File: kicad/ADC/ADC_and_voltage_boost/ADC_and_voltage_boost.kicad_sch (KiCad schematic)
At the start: 11 parts, among them J1 Screw_Terminal_01x04, J2 Screw_Terminal_01x04, J3 Screw_Terminal_01x02, U4 MAX1032BEUG_

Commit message: v3 for ADC up
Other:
- moved on the sheet: A1, C1, C11, C2, C3, C8, C9, J2, U4

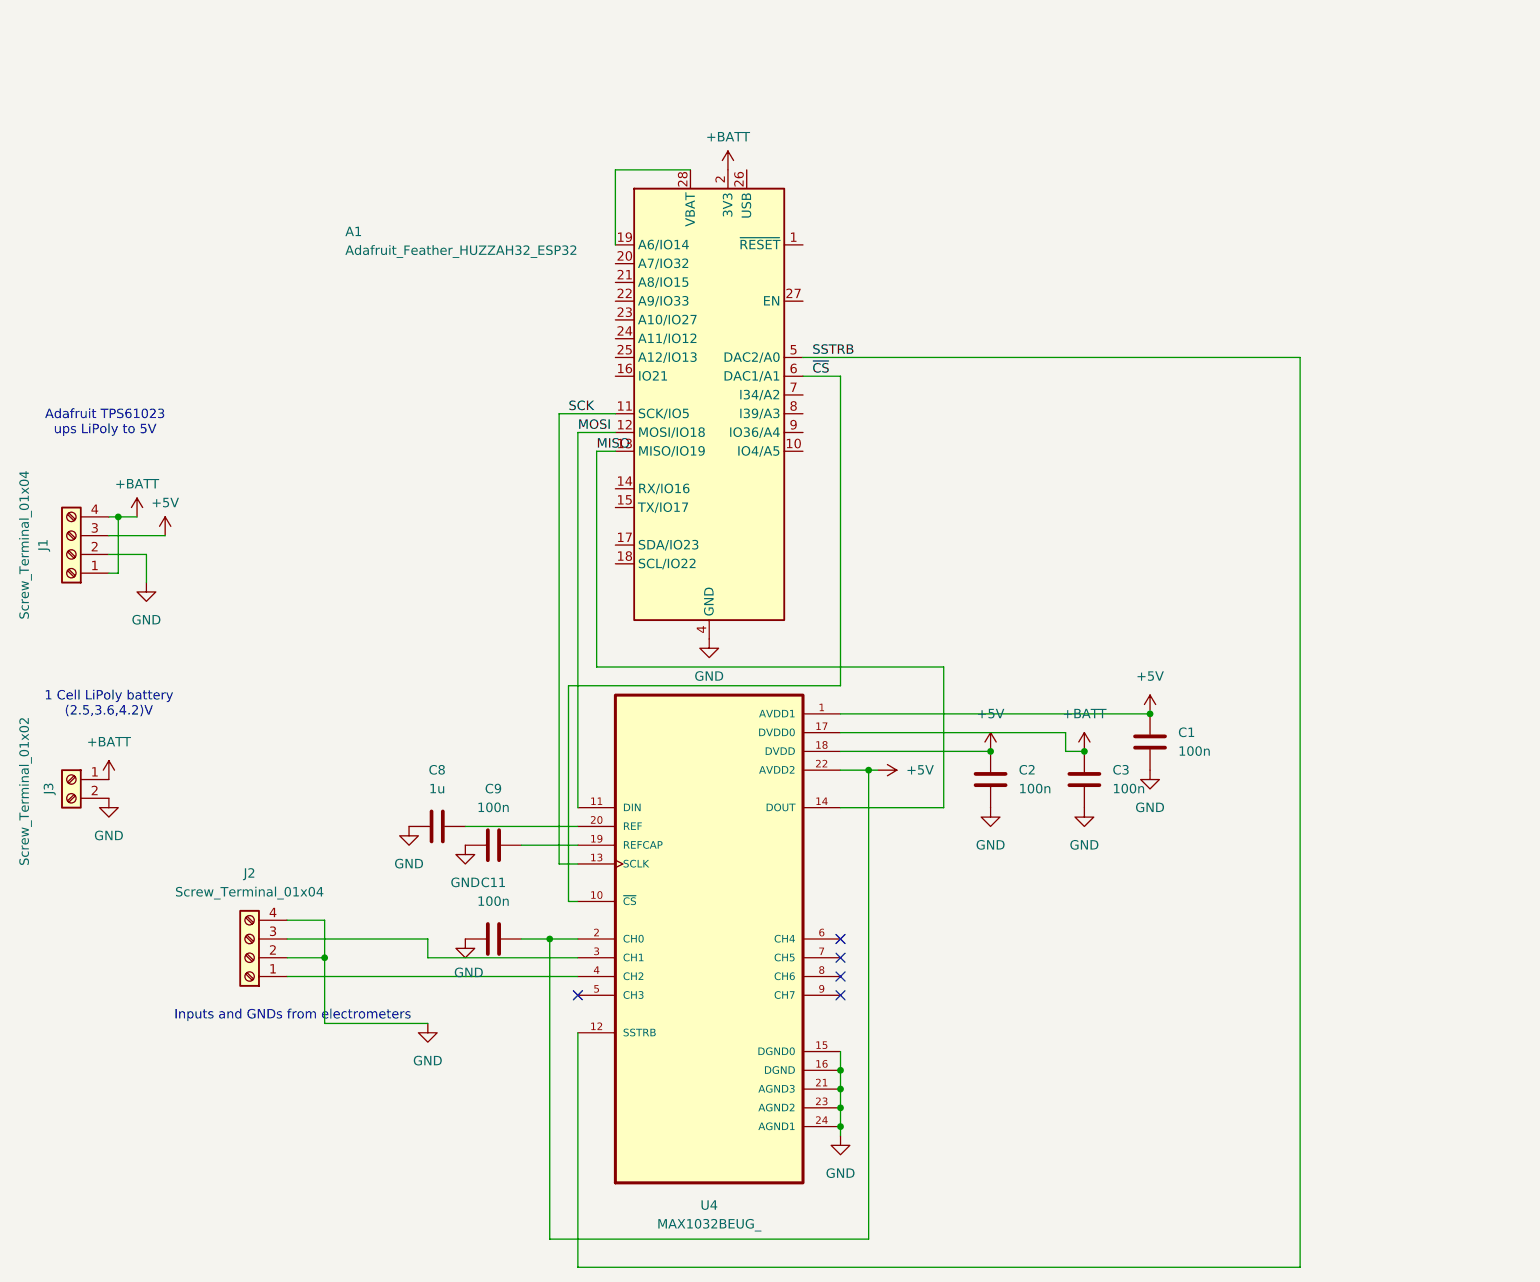
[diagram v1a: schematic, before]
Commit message: switched back to xiao on adc
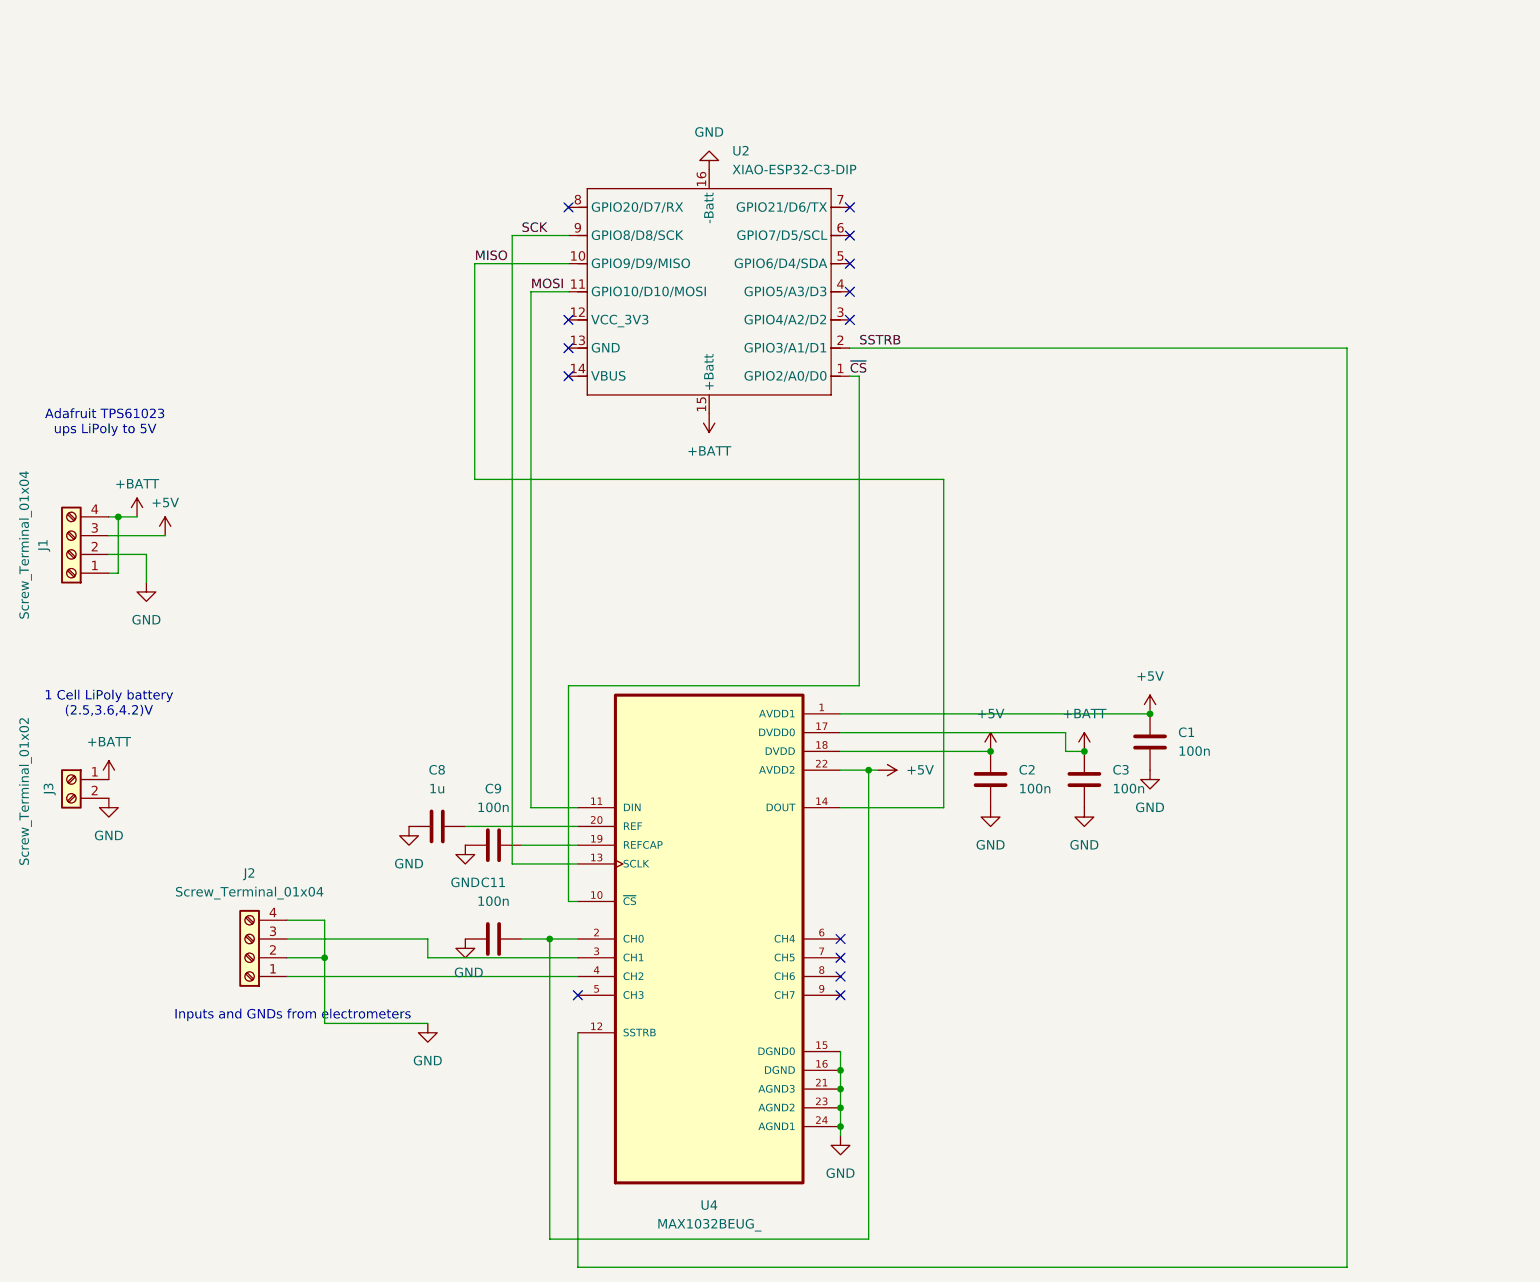
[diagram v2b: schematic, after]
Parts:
- removed A1: Adafruit_Feather_HUZZAH32_ESP32, Module:Adafruit_Feather, symbol MCU_Module:Adafruit_Feather_HUZZAH32_ESP32
- added U2: XIAO-ESP32-C3-DIP, XIAO_DIP:XIAO-ESP32C3-DIP, symbol Seeed_Studio_XIAO_Series:XIAO-ESP32-C3-DIP
- J3: footprint Connector_PinHeader_2.54mm:PinHeader_1x02_P2.54mm_Vertical -> TerminalBlock_Phoenix:TerminalBlock_Phoenix_MPT-0,5-2-2.54_1x02_P2.54mm_Horizontal
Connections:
- net +BATT: now also U2.15 (+Batt)
- net GND: now also U2.16 (-Batt)
- net MISO: now also U2.10 (GPIO9/D9/MISO)
- net MOSI: now also U2.11 (GPIO10/D10/MOSI)
- net SCK: now also U2.9 (GPIO8/D8/SCK)
- net SSTRB: now also U2.2 (GPIO3/A1/D1)
- net ~{CS}: now also U2.1 (GPIO2/A0/D0)
- no-connect marks 5 -> 14
